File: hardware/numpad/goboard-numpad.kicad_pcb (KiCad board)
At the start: 2 copper layers, 38 parts, among them J1 Conn_02x05_Top_Bottom, J2 Conn_01x01, SW10 5, SW12 2, SW13 ., SW14 *, SW15 9, SW16 6, SW17 3, SW18 -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

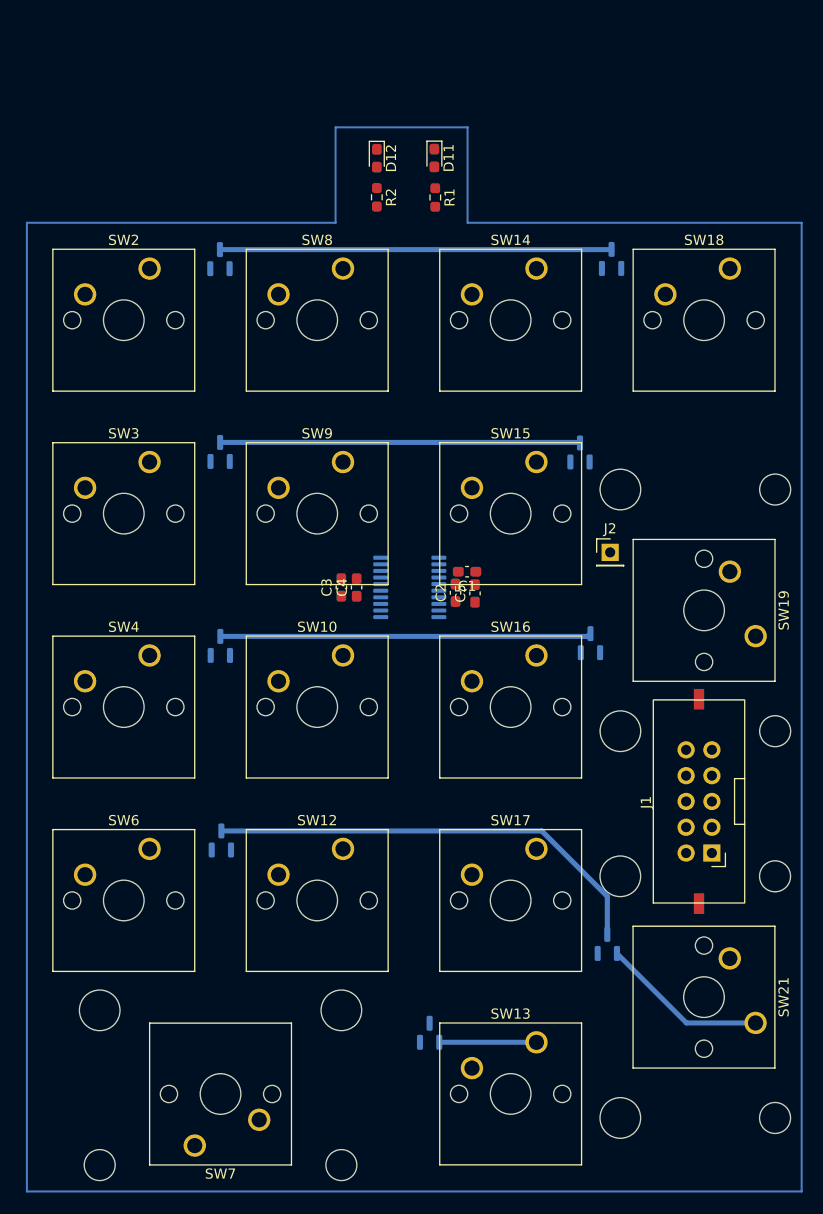
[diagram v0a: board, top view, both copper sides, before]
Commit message: Redo board edge outline
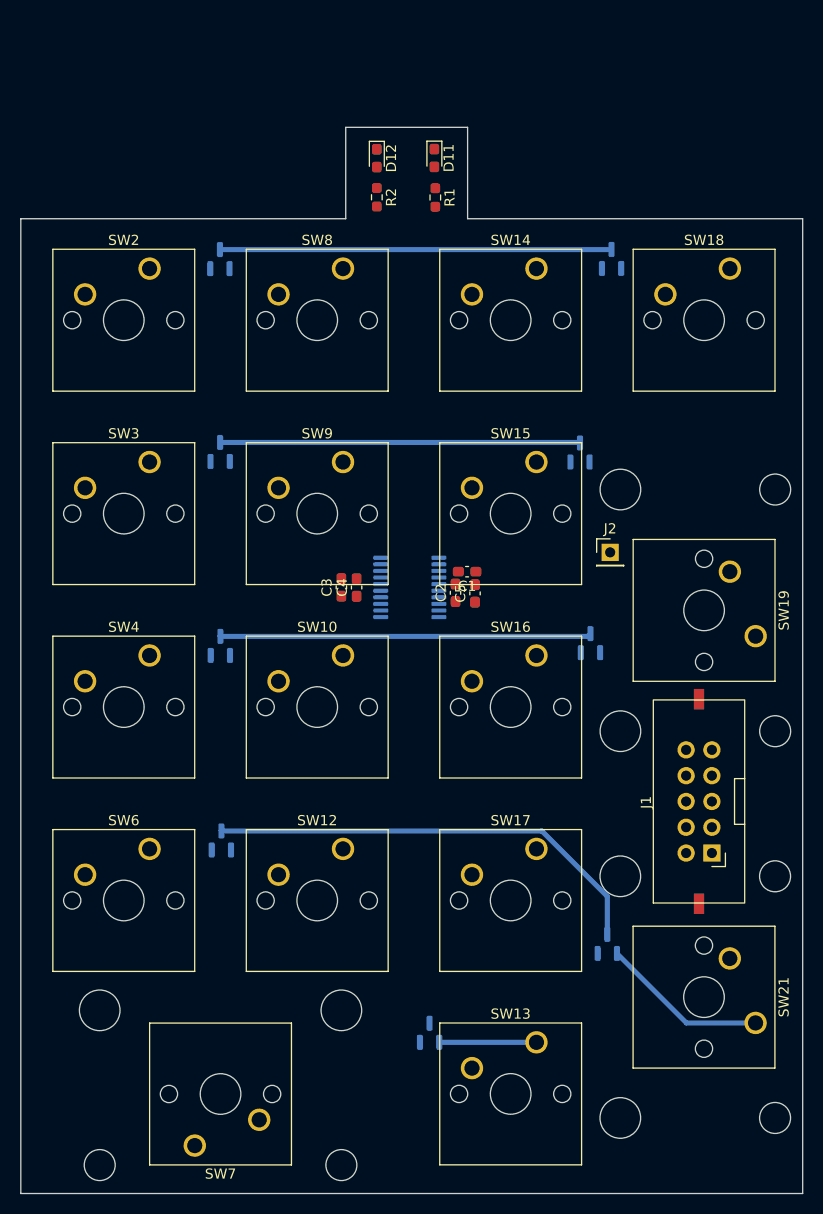
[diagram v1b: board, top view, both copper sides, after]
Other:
- board outline added: 77 x 105 mm
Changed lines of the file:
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@@
     )
   )
-  (gr_line (start 135 57.4) (end 135 48) (layer "B.Cu") (width 0.2))
-  (gr_line (start 135 48) (end 148 48) (layer "B.Cu") (width 0.2))
-  (gr_line (start 180.9 57.4) (end 180.9 152.8) (layer "B.Cu") (width 0.2))
-  (gr_line (start 104.6 57.4) (end 135 57.4) (layer "B.Cu") (width 0.2))
-  (gr_line (start 180.9 152.8) (end 104.6 152.8) (layer "B.Cu") (width 0.2))
-  (gr_line (start 148 57.4) (end 180.9 57.4) (layer "B.Cu") (width 0.2))
-  (gr_line (start 104.6 152.8) (end 104.6 57.4) (layer "B.Cu") (width 0.2))
-  (gr_line (start 148 48) (end 148 57.4) (layer "B.Cu") (width 0.2))
+  (gr_line (start 104 57) (end 136 57) (layer "Edge.Cuts") (width 0.1))
+  (gr_line (start 104 153) (end 104 57) (layer "Edge.Cuts") (width 0.1))
+  (gr_line (start 148 48) (end 148 57) (layer "Edge.Cuts") (width 0.1))
+  (gr_line (start 136 48) (end 148 48) (layer "Edge.Cuts") (width 0.1))
+  (gr_line (start 148 57) (end 181 57) (layer "Edge.Cuts") (width 0.1))
+  (gr_line (start 181 153) (end 104 153) (layer "Edge.Cuts") (width 0.1))
+  (gr_line (start 181 57) (end 181 153) (layer "Edge.Cuts") (width 0.1))
+  (gr_line (start 136 57) (end 136 48) (layer "Edge.Cuts") (width 0.1))
   (segment (start 123.63 79.0325) (end 159.02 79.0325) (width 0.5) (layer "B.Cu") (net 1))
   (segment (start 159.02 79.0325) (end 159.07 79.0825) (width 0.5) (layer "B.Cu") (net 1))

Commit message: Numpad: WIP: design PCB
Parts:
- added J3: Conn_01x05, Connector_PinHeader_2.54mm:PinHeader_1x05_P2.54mm_Vertical, F.Cu at (137.8, 55.0)
- added R3: 1k, Resistor_SMD:R_0603_1608Metric_Pad0.98x0.95mm_HandSolder, F.Cu at (124.2, 39.9)
- added R4: 100k, Resistor_SMD:R_0603_1608Metric_Pad0.98x0.95mm_HandSolder, B.Cu at (112.7, 61.9)
- added R5: 100k, Resistor_SMD:R_0603_1608Metric_Pad0.98x0.95mm_HandSolder, B.Cu at (130.3, 61.8)
- added R6: 100k, Resistor_SMD:R_0603_1608Metric_Pad0.98x0.95mm_HandSolder, B.Cu at (150.4, 62.0)
- added R7: 100k, Resistor_SMD:R_0603_1608Metric_Pad0.98x0.95mm_HandSolder, B.Cu at (169.7, 61.9)
- added SW1: SW_Push, Button_Switch_SMD:SW_SPST_CK_RS282G05A3, F.Cu at (142.6, 108.2)
- C1, C2, C3, C4, C5, R2: moved to B.Cu
- SW13: value . -> dot
- SW14: value * -> times
- SW18: value - -> minus
- SW19: value + -> plus
- SW8: value / -> divide
- moved J1 75.7 mm to (151.5, 46.6), turned to 180 degrees
- moved J2 36.1 mm to (142.8, 120.4)
- moved R2 30.4 mm to (169.4, 53.6)
- moved D12 26.4 mm to (165.3, 53.6), turned to 90 degrees
- moved D11 17.1 mm to (161.7, 53.6), turned to 90 degrees
- moved R1 13.8 mm to (158.6, 53.6)
- moved D7 11.6 mm to (156.5, 71.1)
- moved D2 11.5 mm to (118.2, 90.2)
- moved D3 11.4 mm to (118.6, 109.3)
- moved D1 11.3 mm to (118.3, 71.0)
- moved D5 11.3 mm to (118.4, 128.2)
- moved D9 11.1 mm to (156.6, 109.3)
- moved C5 10.7 mm to (141.8, 102.1), turned to 0 degrees
- moved D6 10.7 mm to (148.2, 147.1)
- moved C1 10.4 mm to (143.9, 101.3), turned to -90 degrees
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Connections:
- net /mcu/COLUMN_0 renamed /Keys/COLUMN_0
- net /mcu/COLUMN_1 renamed /Keys/COLUMN_1
- net /mcu/COLUMN_2 renamed /Keys/COLUMN_2
- net /mcu/COLUMN_3 renamed /Keys/COLUMN_3
- net /mcu/COLUMN_4 renamed /Keys/COLUMN_4
- net /mcu/ROW_0 renamed /Keys/ROW_0
- net /mcu/ROW_1 renamed /Keys/ROW_1
- net /mcu/ROW_2 renamed /Keys/ROW_2
- net /mcu/ROW_3 renamed /Keys/ROW_3
- D9 pad 1: Net-(D9-Pad1) -> unconnected-(D9-Pad1)
- J1 pad 10: no_connect_40 -> unconnected-(J1-Pad10)
- J1 pad 3: no_connect_41 -> unconnected-(J1-Pad3)
- J1 pad 5: no_connect_42 -> unconnected-(J1-Pad5)
- U1 pad 11: /mcu/COLUMN_5 -> unconnected-(U1-Pad11)
- U1 pad 17: /mcu/UART_TX -> /UART_TX
- U1 pad 18: /mcu/UART_RX -> /UART_RX
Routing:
- net VCC: track 0.00 -> 120.9 mm, vias 0 -> 3
- net /Keys/ROW_0: track 0.00 -> 94.6 mm
- net /Keys/ROW_3: track 0.00 -> 71.2 mm, vias 0 -> 4
- net /Keys/ROW_2: track 0.00 -> 61.6 mm
- net /Keys/ROW_1: track 0.00 -> 61.6 mm, vias 0 -> 5
- net /mcu/LED_POWER: track 0.00 -> 59.4 mm, vias 0 -> 6
- net /SWDCLK: track 0.00 -> 57.2 mm, vias 0 -> 4
- net /SWDIO: track 0.00 -> 49.7 mm
- net /UART_RX: track 0.00 -> 41.6 mm
- net /UART_TX: track 0.00 -> 41.2 mm
- net /Keys/COLUMN_2: track 36.6 -> 0.00 mm
- net /mcu/LED_NUMLOCK: track 0.00 -> 31.4 mm, vias 0 -> 1
- net Net-(D8-Pad1): track 0.00 -> 29.5 mm
- net Net-(D6-Pad2): track 0.01 -> 26.5 mm
- net Net-(D1-Pad1): track 0.00 -> 26.0 mm
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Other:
- board size 77 x 105 mm -> 77 x 96 mm

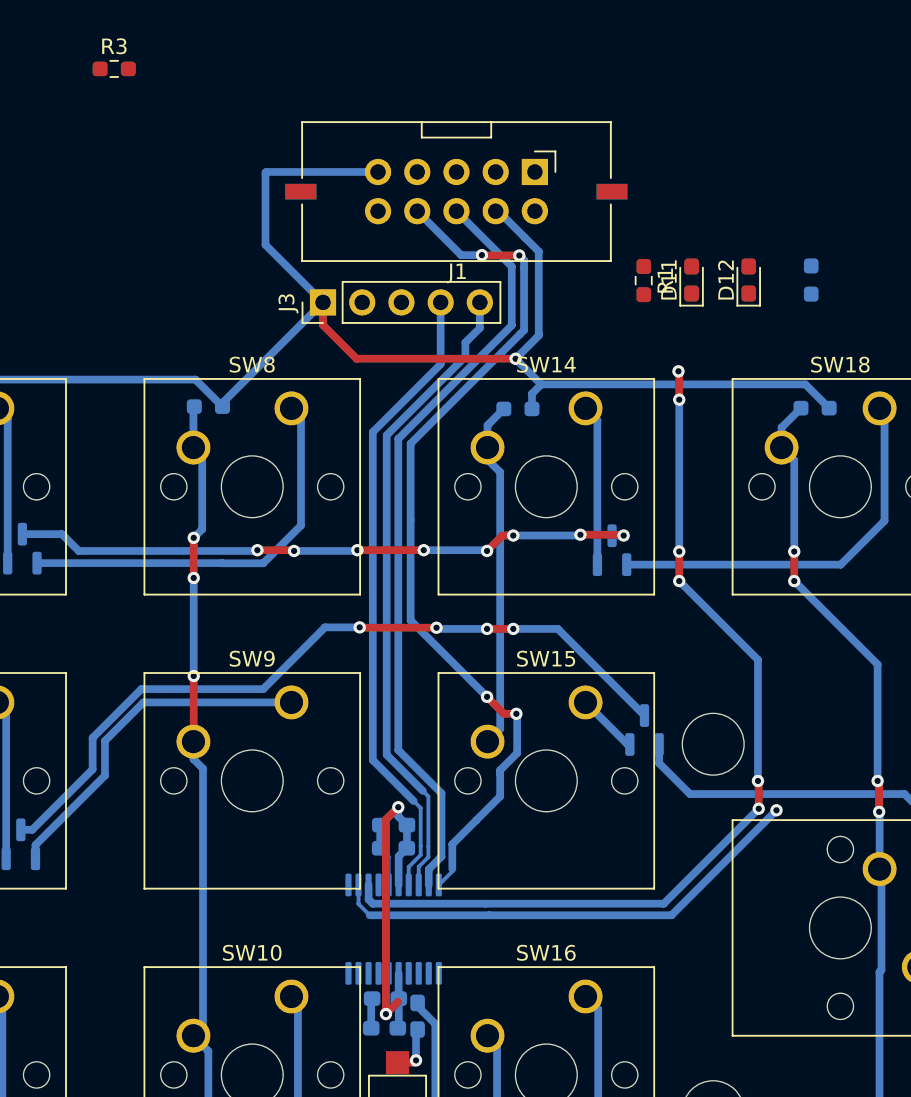
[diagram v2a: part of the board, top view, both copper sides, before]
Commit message: Numpad: Fix labels of columns and rows of the key matrix
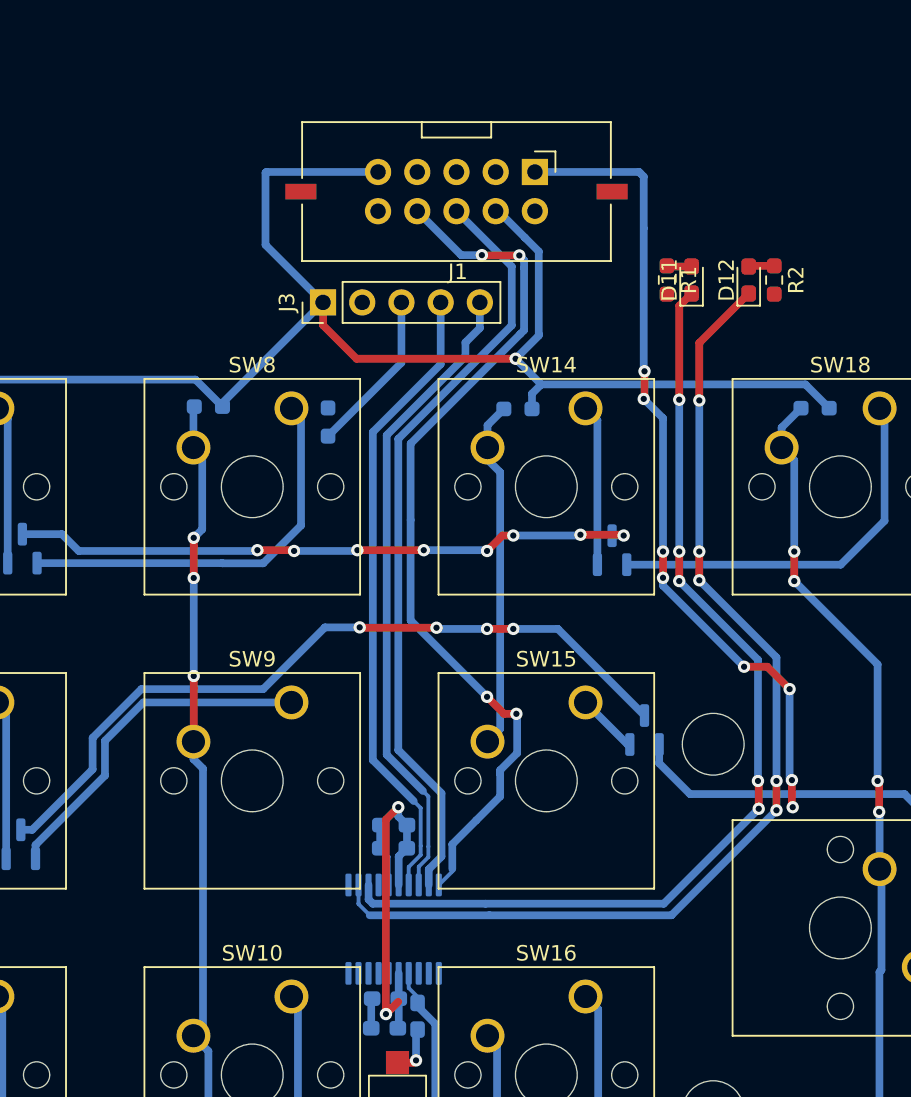
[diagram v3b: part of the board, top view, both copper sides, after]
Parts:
- R2: moved to F.Cu
- R3: moved to B.Cu
- moved R3 26.7 mm to (138.1, 62.8), turned to 90 degrees
- moved R2 2.40 mm to (167.0, 53.6)
- moved R1 1.50 mm to (160.1, 53.6)
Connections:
- U1 pad 12: /mcu/LED_NUMLOCK -> /mcu/LED_POWER
- U1 pad 13: /mcu/LED_POWER -> /mcu/LED_NUMLOCK
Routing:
- net /RESET: track 23.0 -> 78.1 mm, vias 1 -> 9
- net /mcu/LED_NUMLOCK: track 31.4 -> 64.7 mm, vias 1 -> 5
- net Net-(J3-Pad3): track 0.00 -> 10.6 mm
- net /mcu/LED_POWER: track 59.4 -> 68.3 mm, vias 6 -> 5
- net Net-(D12-Pad2): track 0.00 -> 1.67 mm
- net Net-(D11-Pad2): track 0.00 -> 1.62 mm

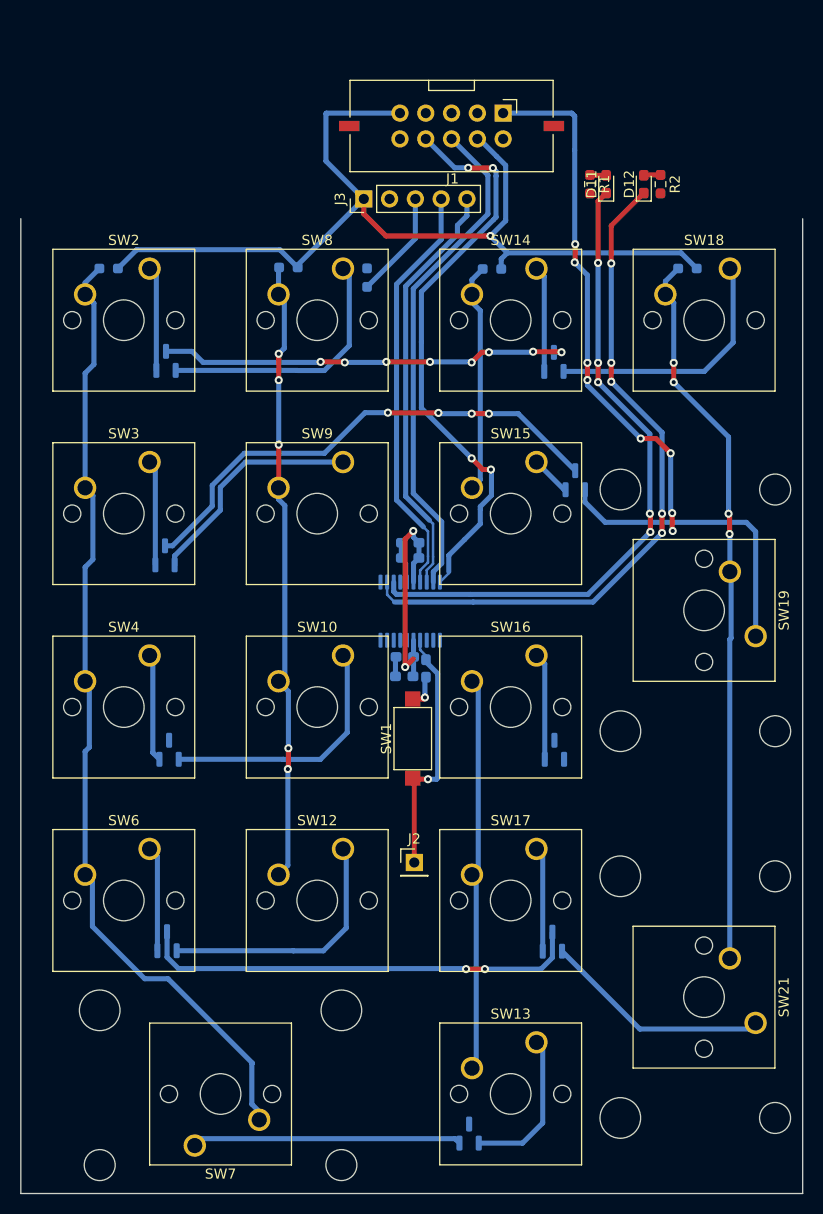
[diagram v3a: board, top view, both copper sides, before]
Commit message: Numpad: Create traces from the MCU to the keymatrix
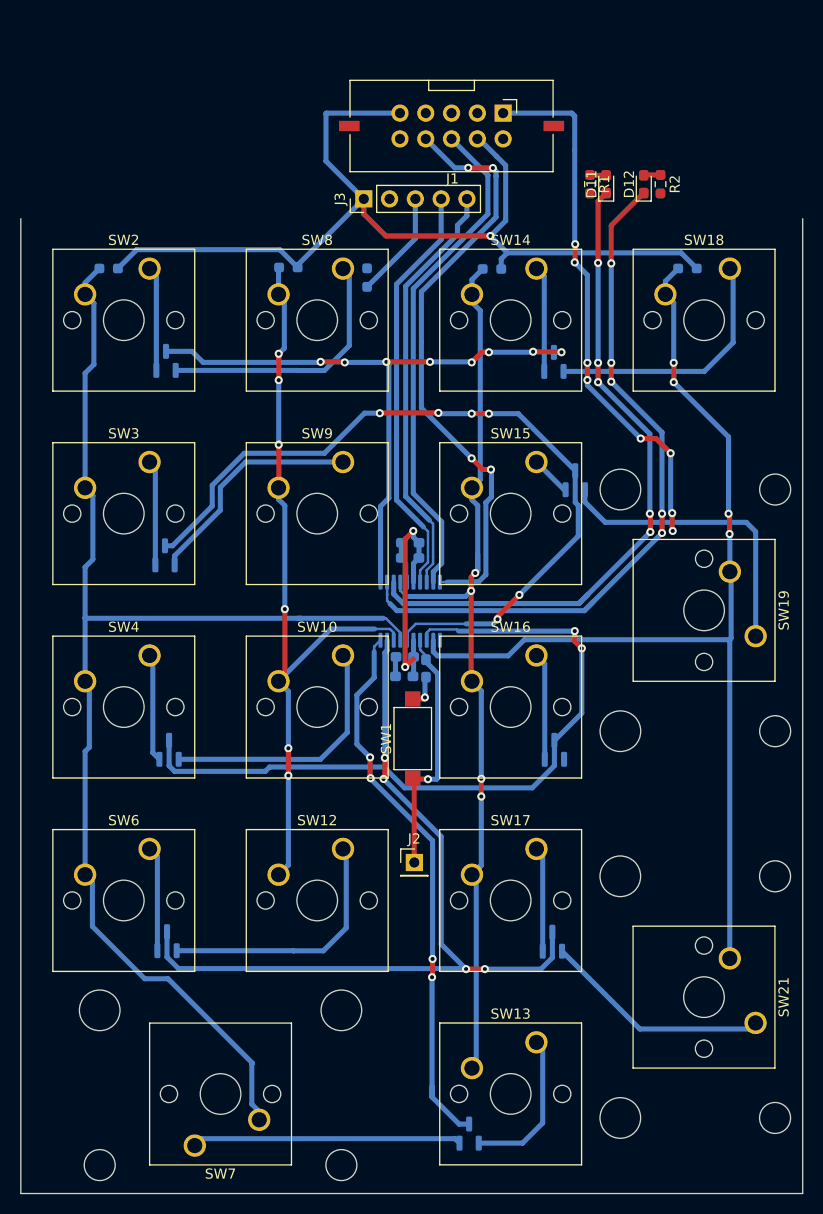
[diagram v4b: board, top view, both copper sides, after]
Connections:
- net /Keys/COLUMN_4 renamed /Keys/ROW_4
- D1 pad 3: /Keys/COLUMN_0 -> /Keys/ROW_0
- D10 pad 3: /Keys/COLUMN_3 -> /Keys/ROW_3
- D2 pad 3: /Keys/COLUMN_1 -> /Keys/ROW_1
- D3 pad 3: /Keys/COLUMN_2 -> /Keys/ROW_2
- D5 pad 3: /Keys/COLUMN_3 -> /Keys/ROW_3
- D7 pad 3: /Keys/COLUMN_0 -> /Keys/ROW_0
- D8 pad 3: /Keys/COLUMN_1 -> /Keys/ROW_1
- D9 pad 3: /Keys/COLUMN_2 -> /Keys/ROW_2
- R4 pad 2: /Keys/ROW_0 -> /Keys/COLUMN_0
- R5 pad 2: /Keys/ROW_1 -> /Keys/COLUMN_1
- R6 pad 2: /Keys/ROW_2 -> /Keys/COLUMN_2
- R7 pad 2: /Keys/ROW_3 -> /Keys/COLUMN_3
- SW10 pad 2: /Keys/ROW_1 -> /Keys/COLUMN_1
- SW12 pad 2: /Keys/ROW_1 -> /Keys/COLUMN_1
- SW13 pad 2: /Keys/ROW_2 -> /Keys/COLUMN_2
- SW14 pad 2: /Keys/ROW_2 -> /Keys/COLUMN_2
- SW15 pad 2: /Keys/ROW_2 -> /Keys/COLUMN_2
- SW16 pad 2: /Keys/ROW_2 -> /Keys/COLUMN_2
- SW17 pad 2: /Keys/ROW_2 -> /Keys/COLUMN_2
- SW18 pad 2: /Keys/ROW_3 -> /Keys/COLUMN_3
- SW19 pad 2: /Keys/ROW_3 -> /Keys/COLUMN_3
- SW2 pad 2: /Keys/ROW_0 -> /Keys/COLUMN_0
- SW21 pad 2: /Keys/ROW_3 -> /Keys/COLUMN_3
- SW3 pad 2: /Keys/ROW_0 -> /Keys/COLUMN_0
- SW4 pad 2: /Keys/ROW_0 -> /Keys/COLUMN_0
- SW6 pad 2: /Keys/ROW_0 -> /Keys/COLUMN_0
- SW7 pad 2: /Keys/ROW_0 -> /Keys/COLUMN_0
- SW8 pad 2: /Keys/ROW_1 -> /Keys/COLUMN_1
- SW9 pad 2: /Keys/ROW_1 -> /Keys/COLUMN_1
- U1 pad 1: /Keys/ROW_3 -> unconnected-(U1-Pad1)
- U1 pad 11: unconnected-(U1-Pad11) -> /Keys/ROW_0
- U1 pad 14: /Keys/ROW_2 -> /Keys/COLUMN_2
- U1 pad 2: /Keys/ROW_0 -> /Keys/COLUMN_3
- U1 pad 3: /Keys/ROW_1 -> /Keys/ROW_2
- U1 pad 6: /Keys/COLUMN_0 -> /Keys/ROW_1
- U1 pad 7: /Keys/COLUMN_1 -> /Keys/COLUMN_0
- U1 pad 8: /Keys/COLUMN_2 -> /Keys/COLUMN_1
- U1 pad 9: /Keys/COLUMN_3 -> /Keys/ROW_3
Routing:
- net /Keys/COLUMN_2: track 0.00 -> 91.8 mm, vias 0 -> 5
- net /Keys/COLUMN_0: track 40.7 -> 127.3 mm, vias 8 -> 0
- net /Keys/COLUMN_3: track 43.9 -> 102.4 mm, vias 2 -> 4
- net /Keys/ROW_4: track 0.00 -> 54.9 mm, vias 0 -> 4
- net /Keys/ROW_0: track 94.6 -> 62.8 mm, vias 0 -> 8
- net /Keys/COLUMN_1: track 49.4 -> 77.0 mm, vias 4 -> 6
- net /Keys/ROW_1: track 61.6 -> 77.6 mm, vias 5 -> 6
- net /Keys/ROW_2: track 61.6 -> 72.8 mm, vias 0 -> 2
- net /Keys/ROW_3: track 71.2 -> 79.8 mm
- net /SWDCLK: track 57.2 -> 60.0 mm
- net /mcu/LED_POWER: track 68.3 -> 70.6 mm
- net /mcu/LED_NUMLOCK: track 64.7 -> 66.9 mm

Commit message: Numpad: Add last traces and ground plane
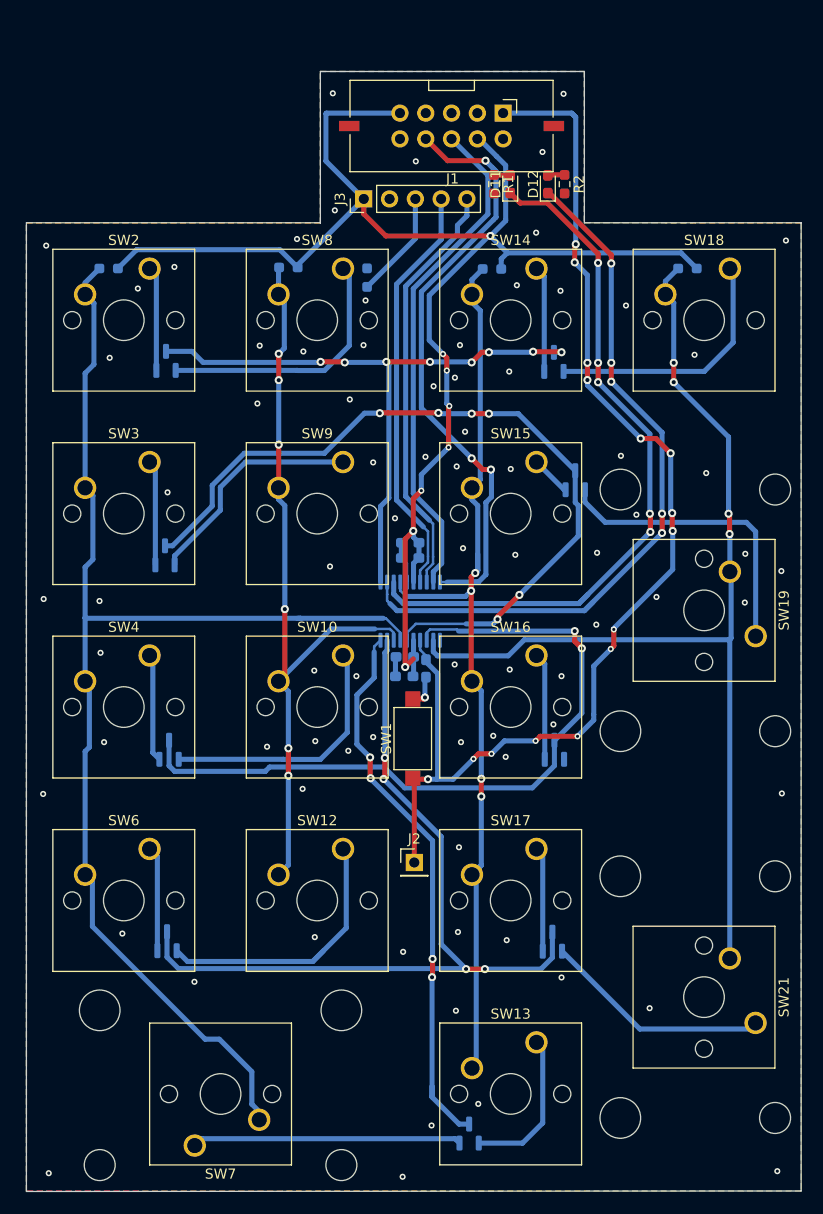
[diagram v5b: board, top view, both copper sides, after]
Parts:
- moved D11 9.45 mm to (152.2, 53.6)
- moved R1 9.45 mm to (150.6, 53.6)
- moved D12 9.45 mm to (155.9, 53.6)
- moved R2 9.45 mm to (157.6, 53.6)
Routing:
- net /RESET: track 78.1 -> 118.3 mm, vias 9 -> 15
- net VCC: track 120.9 -> 154.8 mm, vias 3 -> 8
- net /mcu/LED_NUMLOCK: track 66.9 -> 71.7 mm
- net Net-(D5-Pad1): track 25.6 -> 27.9 mm
- net /mcu/LED_POWER: track 70.6 -> 71.9 mm
- net /Keys/COLUMN_0: track 127.3 -> 126.7 mm
- net GND: vias 1 -> 81
- net /SWDCLK: vias 4 -> 3
- added copper zone on B.Cu, net GND
- added copper zone on F.Cu, net GND
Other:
- board size 77 x 96 mm -> 76.3 x 110.3 mm
